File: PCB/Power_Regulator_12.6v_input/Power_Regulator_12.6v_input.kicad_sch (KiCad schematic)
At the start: 50 parts, among them U2 TPS55340RTER, U3 TPS563203, U4 TPS54JA20RWWR

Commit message: make look nice
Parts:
- removed R17: R30.1k, symbol Device:R
- added R1: R100k, symbol Device:R
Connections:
- net +5V: no longer U3.5 (EN)
- net 5VPGOOD: now reaches U4.9 (PGOOD)
- net 5VPGOOD: now also R1.2
- new net: R1.1, U3.5 (EN)
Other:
- moved on the sheet: C15, C16, C17, C18, C19, C20, C21, C22, C23, C24, C25, C26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

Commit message: dont remember what all is in this commit
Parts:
- removed R12: R169k, symbol Device:R
- added R2: 20k, Resistor_THT:R_Axial_DIN0207_L6.3mm_D2.5mm_P7.62mm_Horizontal, symbol Device:R
- CR1: footprint SMC_DIO -> B540C-13-F:SMC_DIO
- R1, R13, R14, R15, R16, R18, R19, R20, R21, R22, R9: footprint (none) -> Resistor_THT:R_Axial_DIN0207_L6.3mm_D2.5mm_P7.62mm_Horizontal
- R10: value 135k -> 115k; footprint Resistor_SMD:R_0603_1608Metric -> Resistor_THT:R_Axial_DIN0207_L6.3mm_D2.5mm_P7.62mm_Horizontal
- R11: value 30 -> 30k; footprint Resistor_SMD:R_0603_1608Metric -> Resistor_THT:R_Axial_DIN0207_L6.3mm_D2.5mm_P7.62mm_Horizontal
- U2: footprint RTE0016C -> TPS55340RTER:RTE0016C_NV
- U4: footprint RWW0021A -> TPS54JA20RWWR:RWW0021A
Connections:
- net +BATT: now also U2.3 (EN)
- net at C33.2, R11.1, U3.6 (FB): now also R2.2; no longer R10.2
- new net: R10.2, R2.1
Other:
- moved on the sheet: R11

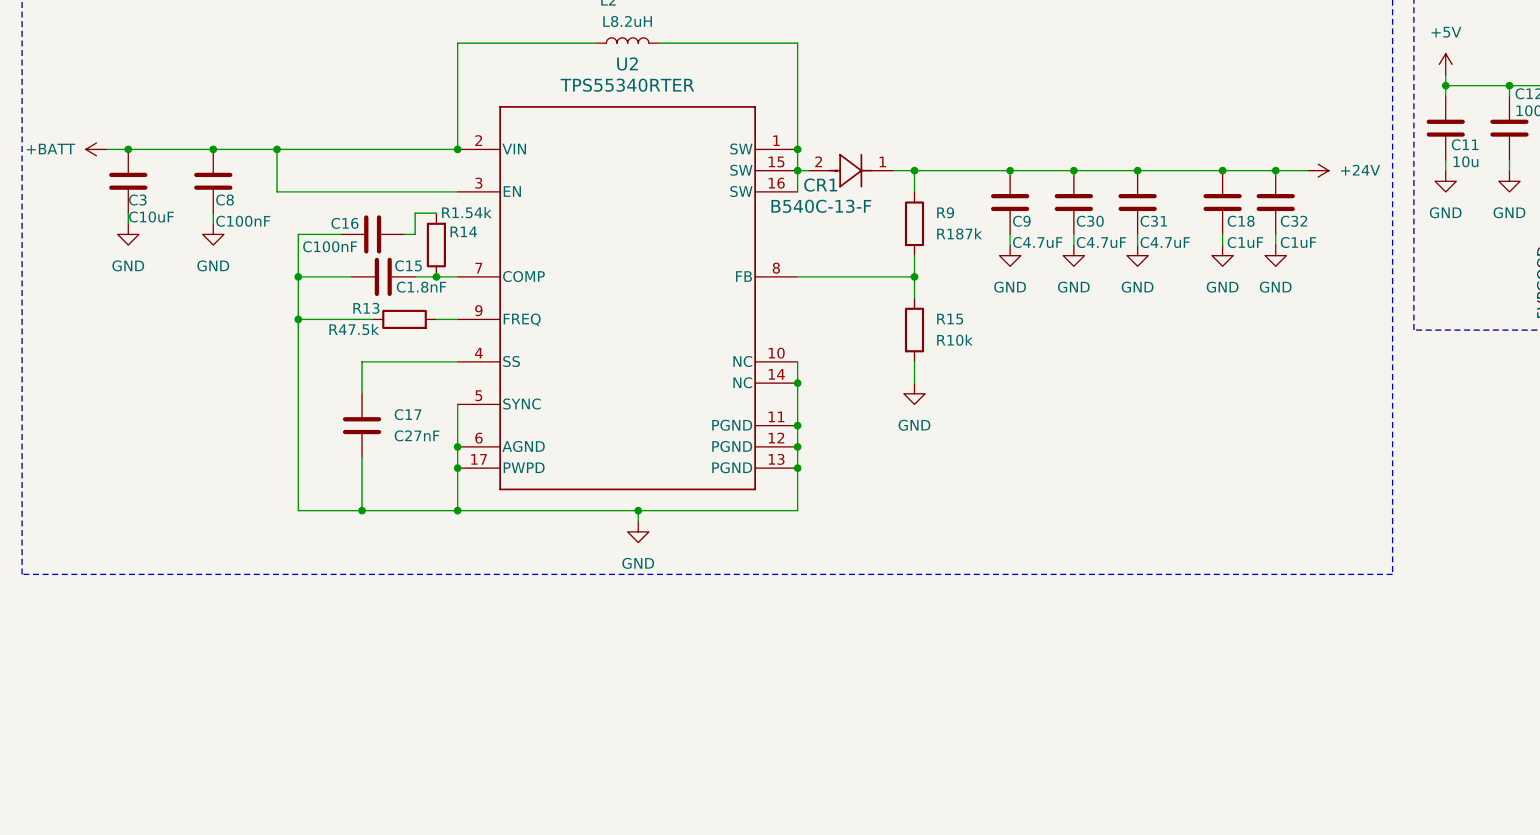
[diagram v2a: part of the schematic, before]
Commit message: Updated power regulator to add SSR to output for switching 24v off
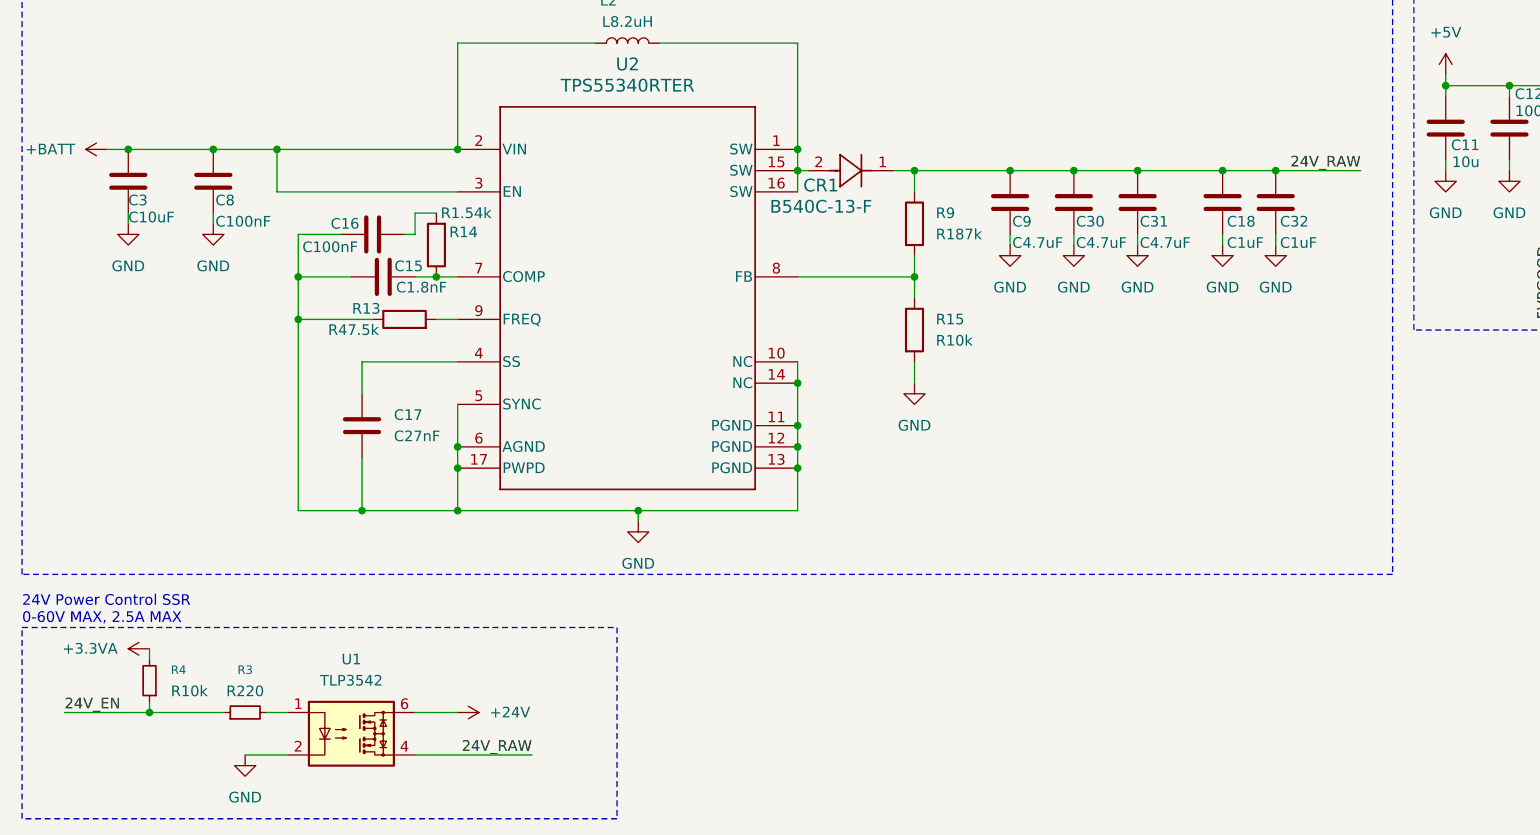
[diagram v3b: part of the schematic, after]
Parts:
- added R3: R220, symbol Device:R_Small
- added R4: R10k, symbol Device:R_Small
- added U1: TLP3542, Package_DIP:DIP-5-6_W7.62mm, symbol Relay_SolidState:TLP3542
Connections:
- net +24V: now also U1.6; no longer C18.1, C30.1, C31.1, C32.1, C9.1, CR1.1, R9.1
- net +3.3VA: now also R4.2
- net GND: now also U1.2
- new net: R3.2, U1.1
- new net 24V_EN: R3.1, R4.1
- new net 24V_RAW: C18.1, C30.1, C31.1, C32.1, C9.1, CR1.1, R9.1, U1.4
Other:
- note added: "24V Power Control SSR 0-60V MAX, 2.5A MAX"

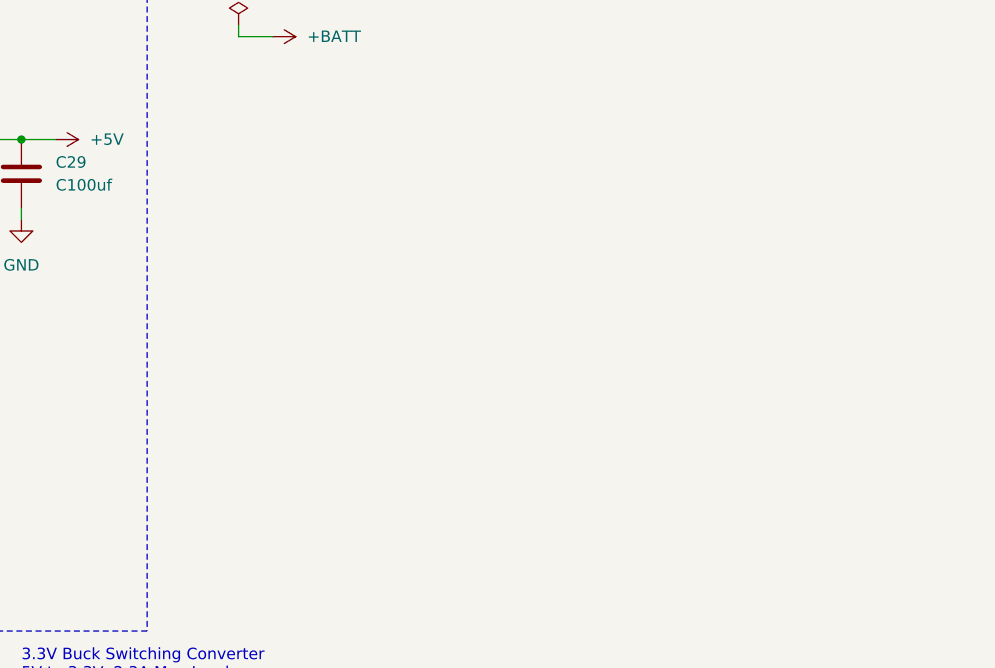
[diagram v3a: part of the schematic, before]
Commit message: added connector to schematic
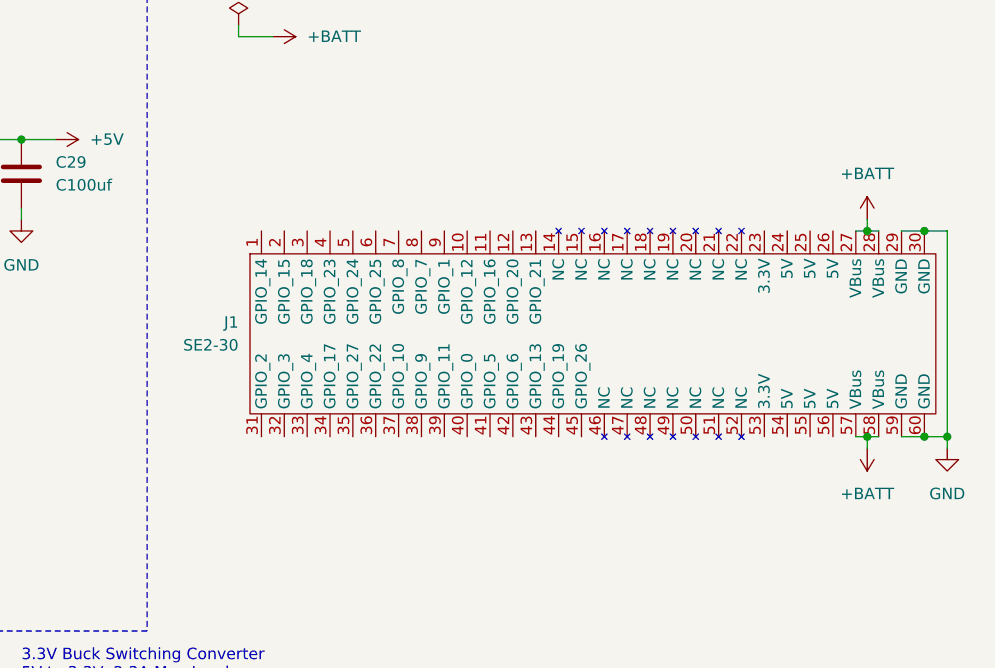
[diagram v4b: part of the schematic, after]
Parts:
- added J1: SE2-30, SE2-30:SE2-30, symbol SE2-30:SE2-30
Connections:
- net +BATT: now also J1.27 (VBus), J1.28 (VBus), J1.57 (VBus), J1.58 (VBus)
- net GND: now also J1.29 (GND), J1.30 (GND), J1.59 (GND), J1.60 (GND)

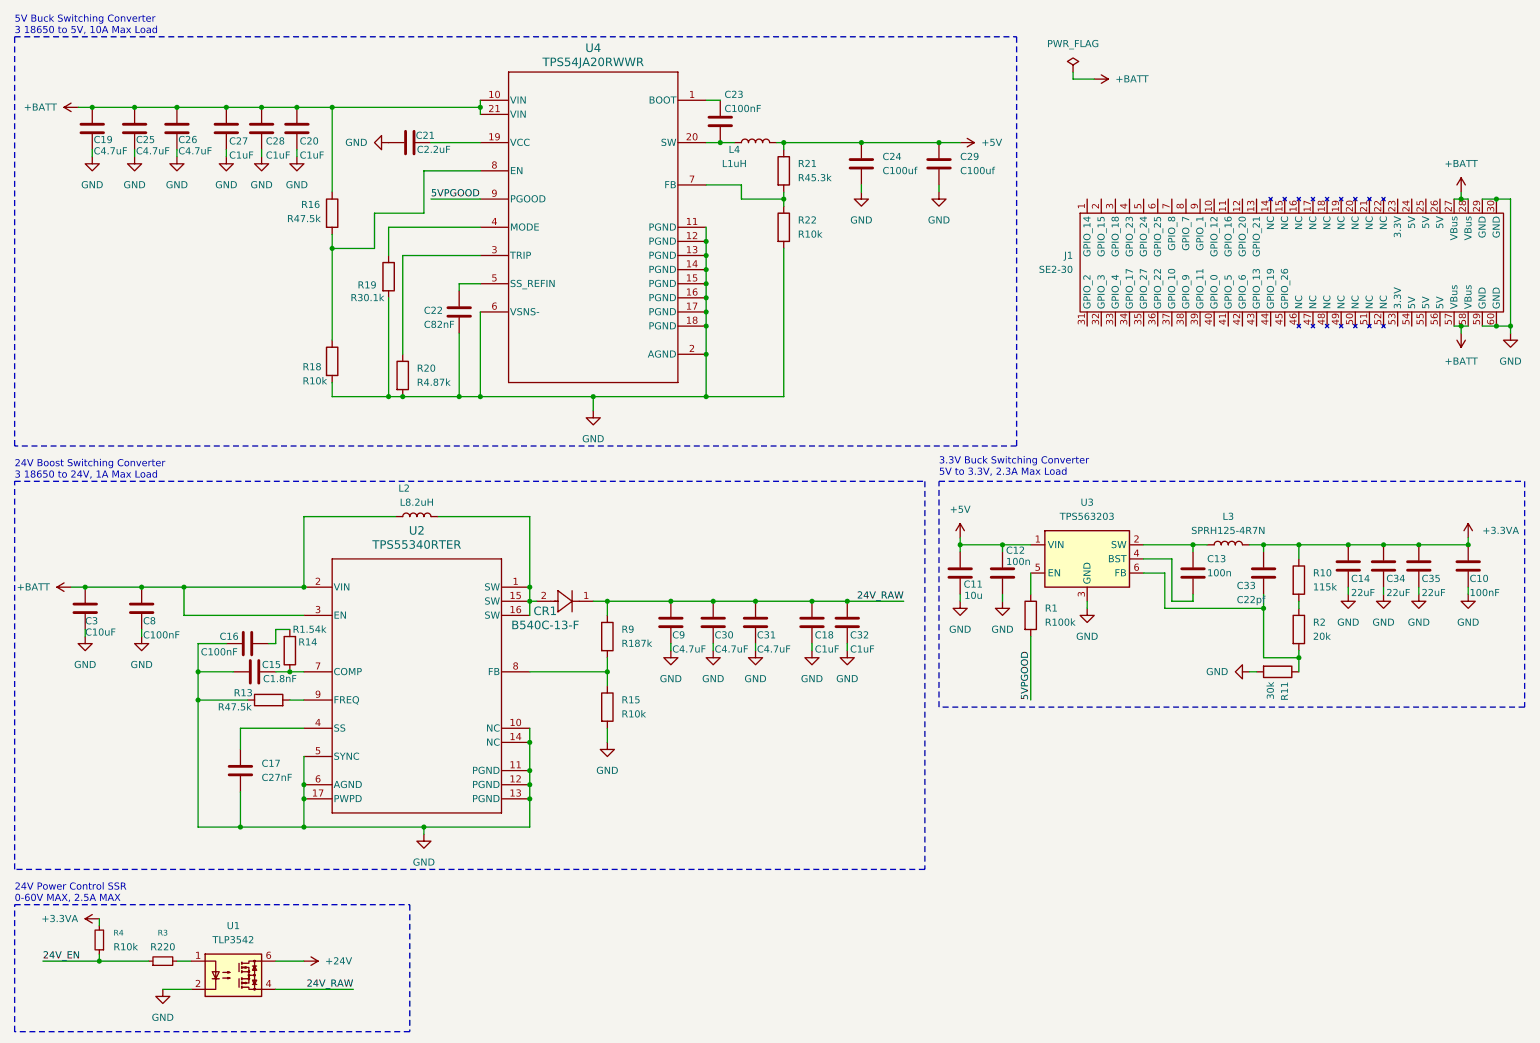
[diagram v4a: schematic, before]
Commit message: added 24v connector and wired connector
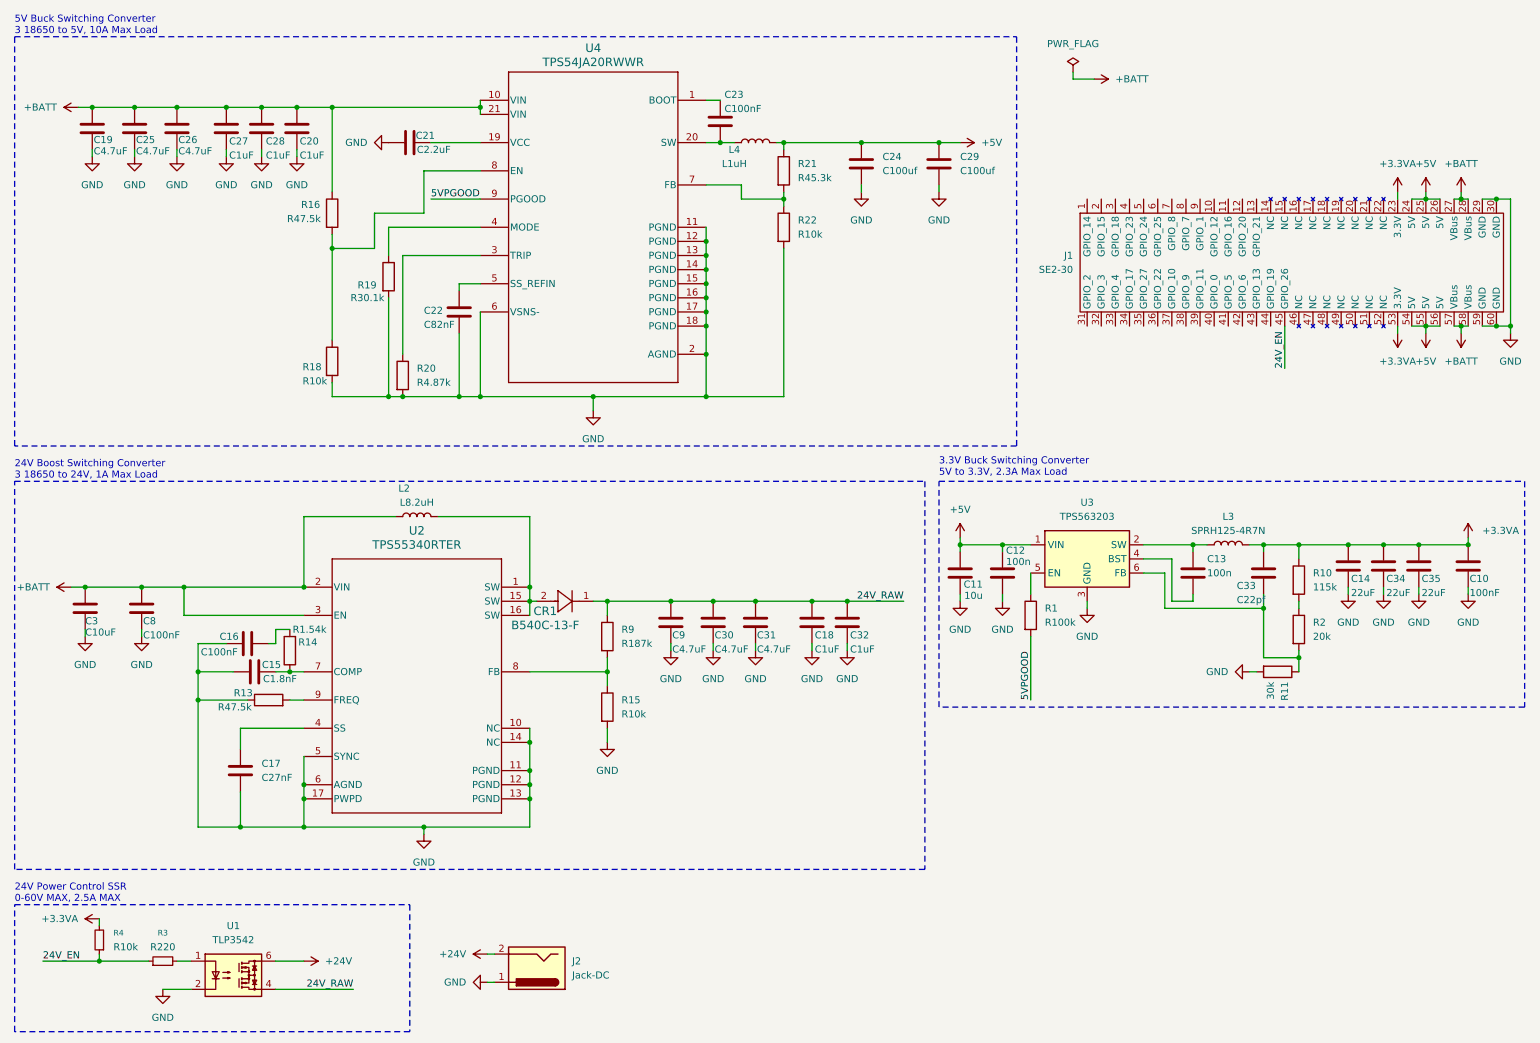
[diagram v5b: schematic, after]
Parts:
- added J2: Jack-DC, symbol Connector:Jack-DC
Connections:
- net +24V: now also J2.2
- net +3.3VA: now also J1.23 (3.3V), J1.53 (3.3V)
- net +5V: now also J1.24 (5V), J1.25 (5V), J1.26 (5V), J1.54 (5V), J1.55 (5V), J1.56 (5V)
- net 24V_EN: now also J1.45 (GPIO_26)
- net GND: now also J2.1

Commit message: assigned footprints to capacitors, preliminary placement of components on pcb
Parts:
- C15, C16, C17, C18, C19, C20, C21, C22, C23, C25, C26, C27, C28, C3, C30, C31, C32, C33, C8, C9: footprint (none) -> Capacitor_SMD:C_0603_1608Metric
- C24, C29: footprint (none) -> Capacitor_SMD:C_1206_3216Metric
- L2, L4: footprint (none) -> Inductor_SMD:L_0603_1608Metric
- L3: footprint Unify:IND_BOURNS_SRN6045 -> Inductor_SMD:L_12x12mm_H6mm
- R3, R4: footprint (none) -> Resistor_THT:R_Axial_DIN0207_L6.3mm_D2.5mm_P7.62mm_Horizontal
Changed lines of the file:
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@@
 			)
 		)
-		(property "Footprint" ""
+		(property "Footprint" "Capacitor_SMD:C_0603_1608Metric"
 			(at 52.3748 146.05 0)
 			(effects
@@
 			)
 		)
-		(property "Footprint" ""
+		(property "Footprint" "Capacitor_SMD:C_0603_1608Metric"
 			(at 93.6752 71.12 0)
 			(effects
@@
 			)
 		)
-		(property "Footprint" ""
+		(property "Footprint" "Capacitor_SMD:C_1206_3216Metric"
 			(at 166.0652 44.45 0)
 			(effects
@@
 			)
 		)
-		(property "Footprint" ""
+		(property "Footprint" "Capacitor_SMD:C_0603_1608Metric"
 			(at 35.2552 38.1 0)
 			(effects
@@
 			)
 		)
-		(property "Footprint" ""
+		(property "Footprint" "Resistor_THT:R_Axial_DIN0207_L6.3mm_D2.5mm_P7.62mm_Horizontal"
 			(at 39.37 184.15 0)
 			(effects
@@
 			)
 		)
-		(property "Footprint" ""
+		(property "Footprint" "Capacitor_SMD:C_0603_1608Metric"
 			(at 238.4552 118.11 0)
 			(effects
@@
 			)
 		)
-		(property "Footprint" ""
+		(property "Footprint" "Capacitor_SMD:C_0603_1608Metric"
 			(at 163.5252 127 0)
 			(effects
@@
 			)
 		)
-		(property "Footprint" ""
+		(property "Footprint" "Capacitor_SMD:C_0603_1608Metric"
 			(at 131.7752 127 0)
 			(effects
@@
 			)
 		)
-		(property "Footprint" ""
+		(property "Footprint" "Capacitor_SMD:C_0603_1608Metric"
 			(at 26.3652 124.46 0)
 			(effects
@@
 			)
 		)
-		(property "Footprint" "Unify:IND_BOURNS_SRN6045"
+		(property "Footprint" "Inductor_SMD:L_12x12mm_H6mm"
 			(at 231.14 109.22 0)
 			(effects
@@
 			)
 		)
-		(property "Footprint" ""
+		(property "Footprint" "Capacitor_SMD:C_0603_1608Metric"
 			(at 147.0152 127 0)
 			(effects
@@
 			)
 		)
-		(property "Footprint" ""
+		(property "Footprint" "Capacitor_SMD:C_0603_1608Metric"
 			(at 58.42 126.0348 0)
 			(effects
@@
 			)
 		)
-		(property "Footprint" ""
+		(property "Footprint" "Capacitor_SMD:C_0603_1608Metric"
 			(at 139.3952 127 0)
 			(effects
@@
 			)
 		)
-		(property "Footprint" ""
+		(property "Footprint" "Capacitor_SMD:C_0603_1608Metric"
 			(at 138.7348 29.21 0)
 			(effects
@@
 			)
 		)
-		(property "Footprint" ""
+		(property "Footprint" "Inductor_SMD:L_0603_1608Metric"
 			(at 85.09 104.14 0)
 			(effects
@@
 			)
 		)
-		(property "Footprint" ""
+		(property "Footprint" "Capacitor_SMD:C_0603_1608Metric"
 			(at 64.4652 38.1 0)
 			(effects
@@
 			)
 		)
-		(property "Footprint" ""
+		(property "Footprint" "Resistor_THT:R_Axial_DIN0207_L6.3mm_D2.5mm_P7.62mm_Horizontal"
 			(at 27.94 180.34 0)
 			(effects
@@
 			)
 		)
-		(property "Footprint" ""
+		(property "Footprint" "Capacitor_SMD:C_0603_1608Metric"
 			(at 87.63 35.8648 0)
 			(effects
@@
 			)
 		)
-		(property "Footprint" ""
+		(property "Footprint" "Capacitor_SMD:C_0603_1608Metric"
 			(at 58.1152 38.1 0)
 			(effects
@@
 			)
 		)
-		(property "Footprint" ""
+		(property "Footprint" "Capacitor_SMD:C_0603_1608Metric"
 			(at 157.1752 127 0)
 			(effects
@@
 			)
 		)
-		(property "Footprint" ""
+		(property "Footprint" "Capacitor_SMD:C_0603_1608Metric"
 			(at 59.69 131.1148 0)
 			(effects
@@
 			)
 		)
-		(property "Footprint" ""
+		(property "Footprint" "Capacitor_SMD:C_0603_1608Metric"
 			(at 51.7652 38.1 0)
 			(effects
@@
 			)
 		)
-		(property "Footprint" ""
+		(property "Footprint" "Capacitor_SMD:C_0603_1608Metric"
 			(at 27.6352 38.1 0)
 			(effects
@@
 			)
 		)
-		(property "Footprint" ""
+		(property "Footprint" "Capacitor_SMD:C_0603_1608Metric"
 			(at 42.8752 38.1 0)
 			(effects
@@
 			)
 		)
-		(property "Footprint" ""
+		(property "Footprint" "Capacitor_SMD:C_1206_3216Metric"
 			(at 180.0352 44.45 0)
 			(effects
@@
 			)
 		)
-		(property "Footprint" ""
+		(property "Footprint" "Inductor_SMD:L_0603_1608Metric"
 			(at 146.05 36.83 0)
 			(effects
@@
 			)
 		)
-		(property "Footprint" ""
+		(property "Footprint" "Capacitor_SMD:C_0603_1608Metric"
 			(at 36.5252 124.46 0)
 			(effects
